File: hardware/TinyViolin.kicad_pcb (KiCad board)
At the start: 2 copper layers, 100 x 80 mm, 43 parts, among them J1 ICSP, J2 503182-1852, SW1 SW_SPDT, SW2 Tactile, SW3 SW_Push, SW4 SW_Push, SW5 SW_Push, SW6 SW_Push, U1 ATmega328-PU, U2 BOOST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

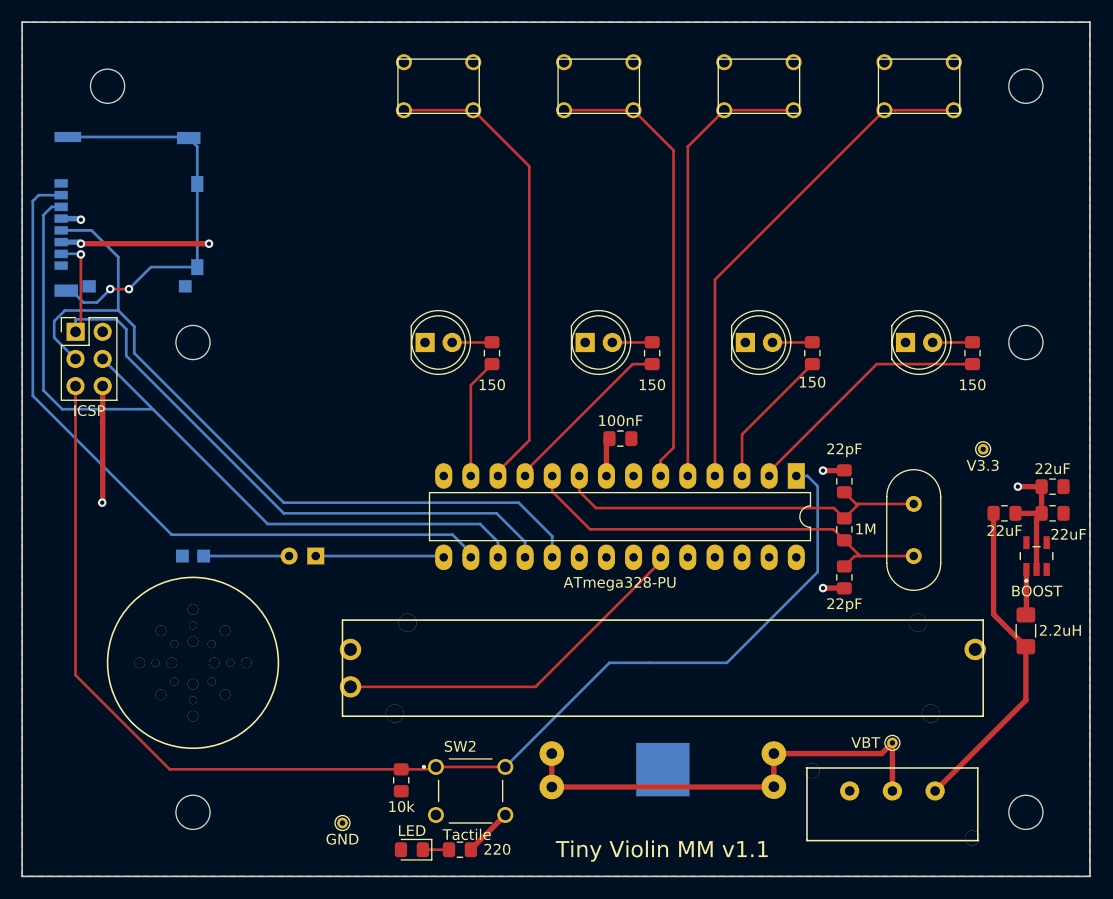
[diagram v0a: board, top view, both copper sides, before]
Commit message: Prepared pcb for re-manufacturing
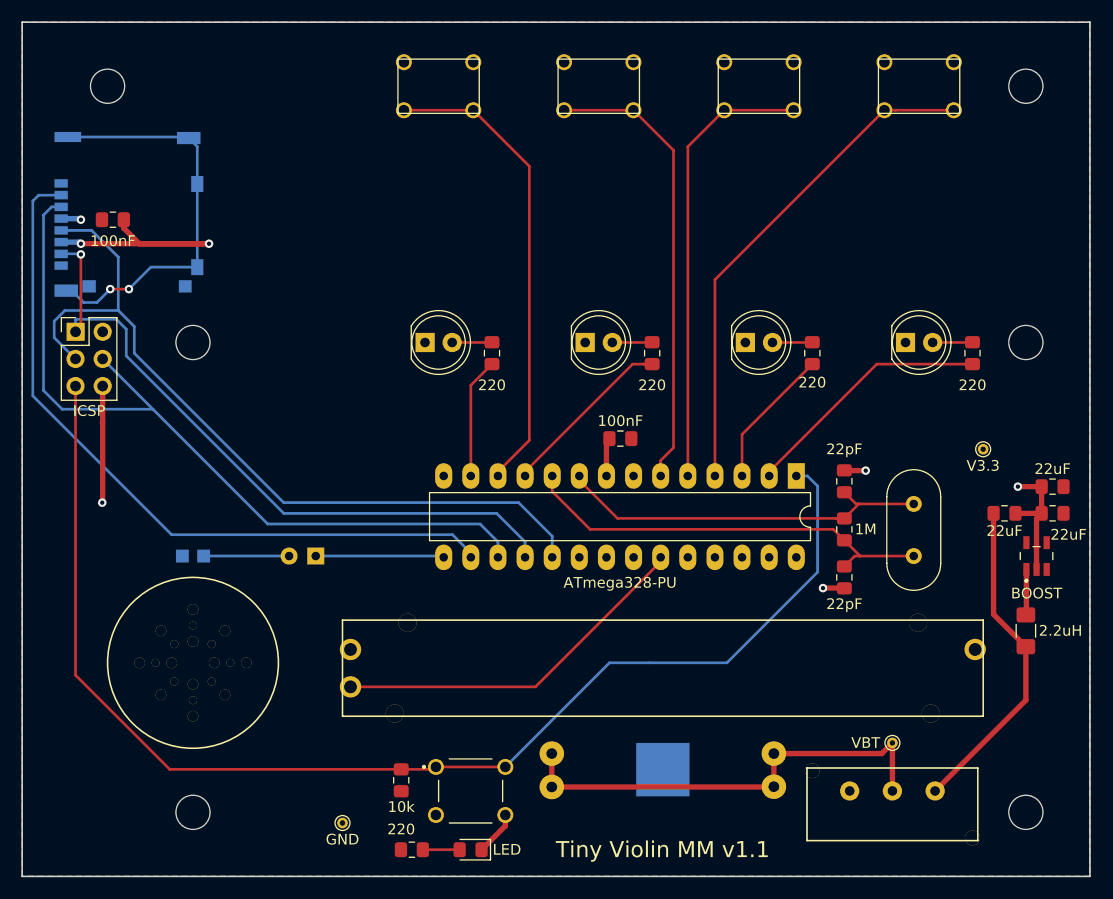
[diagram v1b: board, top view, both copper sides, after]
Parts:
- added C7: 100nF, Capacitor_SMD:C_0805_2012Metric_Pad1.15x1.40mm_HandSolder, F.Cu at (28.5, 38.5)
- BT1: footprint BAT-HLD-001-THM:LINX_BAT-HLD-001-THM -> LINX_BAT-HLD-001-THM
- J2: footprint 503182-1852:MOLEX_503182-1852 -> MOLEX_503182-1852
- R4, R5, R6, R7: value 150 -> 220
- SW2: footprint 1825910-7:SW_1825910-7 -> SW_1825910-7
- U2: footprint TPS613222ADBVT:SOT95P280X145-5N -> SOT95P280X145-5N
- moved D2 5.50 mm to (62.0, 97.5)
- moved R3 4.50 mm to (56.5, 97.5)
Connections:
- D2 pad 1: Net-(D2-Pad1) -> GND
- D2 pad 2: +3V3 -> Net-(D2-Pad2)
- H1 pad 1: (no net) -> Net-(H1-Pad1)
- H2 pad 1: (no net) -> Net-(H2-Pad1)
- H3 pad 1: (no net) -> Net-(H3-Pad1)
- H4 pad 1: (no net) -> Net-(H4-Pad1)
- H5 pad 1: (no net) -> Net-(H5-Pad1)
- H6 pad 1: (no net) -> Net-(H6-Pad1)
- J1 pad 2: (no net) -> Net-(J1-Pad2)
- J2 pad 1: (no net) -> Net-(J2-Pad1)
- J2 pad 8: (no net) -> Net-(J2-Pad8)
- J2 pad DT: (no net) -> Net-(J2-PadDT)
- J2 pad SW: (no net) -> Net-(J2-PadSW)
- R3 pad 1: Net-(D2-Pad1) -> +3V3
- R3 pad 2: GND -> Net-(D2-Pad2)
- SW1 pad 1: (no net) -> Net-(SW1-Pad1)
- U1 pad 14: (no net) -> Net-(U1-Pad14)
- U1 pad 21: (no net) -> Net-(U1-Pad21)
- U1 pad 24: (no net) -> Net-(U1-Pad24)
- U1 pad 25: (no net) -> Net-(U1-Pad25)
- U1 pad 26: (no net) -> Net-(U1-Pad26)
- U1 pad 27: (no net) -> Net-(U1-Pad27)
- U1 pad 28: (no net) -> Net-(U1-Pad28)
- U2 pad 3: (no net) -> Net-(U2-Pad3)
- U2 pad 5: (no net) -> Net-(U2-Pad5)
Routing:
- net GND: track 50.5 -> 58.9 mm
- net Net-(D2-Pad2): track 0.00 -> 3.45 mm
- net Net-(D2-Pad1): track 2.45 -> 0.00 mm
- net Net-(C2-Pad1): track 36.6 -> 35.6 mm

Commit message: Got main thing working
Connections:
- J1 pad 2: Net-(J1-Pad2) -> +3V3
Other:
- board text added: "Tiny Violin MM v1.2"
- board text removed: "Tiny Violin MM v1.1"
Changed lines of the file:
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@@
     (zones 0)
     (modules 44)
-    (nets 51)
+    (nets 50)
   )
   (page A4)
@@
   (net 41 "Net-(H1-Pad1)")
   (net 42 "Net-(SW1-Pad1)")
-  (net 43 "Net-(J1-Pad2)")
-  (net 44 "Net-(U2-Pad3)")
-  (net 45 "Net-(U2-Pad5)")
-  (net 46 "Net-(J2-Pad1)")
-  (net 47 "Net-(J2-Pad8)")
-  (net 48 "Net-(J2-PadSW)")
-  (net 49 "Net-(J2-PadDT)")
-  (net 50 "Net-(D2-Pad2)")
+  (net 43 "Net-(U2-Pad3)")
+  (net 44 "Net-(U2-Pad5)")
+  (net 45 "Net-(J2-Pad1)")
+  (net 46 "Net-(J2-Pad8)")
+  (net 47 "Net-(J2-PadSW)")
+  (net 48 "Net-(J2-PadDT)")
+  (net 49 "Net-(D2-Pad2)")
   (net_class Default "This is the default net class."
     (clearance 0.2)
@@
     (add_net "Net-(H5-Pad1)")
     (add_net "Net-(H6-Pad1)")
-    (add_net "Net-(J1-Pad2)")
     (add_net "Net-(J2-Pad1)")
     (add_net "Net-(J2-Pad8)")
@@
     (fp_circle (center -3.81 8.89) (end -3.71 8.89) (layer B.SilkS) (width 0.2))
     (pad 1 smd rect (at -2.9 6.355 270) (size 0.8 1.24) (layers B.Cu B.Paste B.Mask)
-      (net 46 "Net-(J2-Pad1)"))
+      (net 45 "Net-(J2-Pad1)"))
     (pad 2 smd rect (at -1.8 6.355 270) (size 0.8 1.24) (layers B.Cu B.Paste B.Mask)
       (net 3 /SS))
@@
       (net 4 /MISO))
     (pad 8 smd rect (at 4.8 6.355 270) (size 0.8 1.24) (layers B.Cu B.Paste B.Mask)
-      (net 47 "Net-(J2-Pad8)"))
+      (net 46 "Net-(J2-Pad8)"))
     (pad P1 smd rect (at -7.245 5.725 270) (size 0.95 2.5) (layers B.Cu B.Paste B.Mask)
       (net 16 "Net-(J2-PadP1)"))
@@
       (net 16 "Net-(J2-PadP1)"))
     (pad SW smd rect (at 6.74 3.725 270) (size 1.16 1.25) (layers B.Cu B.Paste B.Mask)
-      (net 48 "Net-(J2-PadSW)"))
+      (net 47 "Net-(J2-PadSW)"))
     (pad DT smd rect (at 6.74 -5.275 270) (size 1.16 1.2) (layers B.Cu B.Paste B.Mask)
-      (net 49 "Net-(J2-PadDT)"))
+      (net 48 "Net-(J2-PadDT)"))
     (pad P3 smd rect (at -7.145 -5.605 270) (size 1.15 2.2) (layers B.Cu B.Paste B.Mask)
       (net 16 "Net-(J2-PadP1)"))
@@
       (net 9 GND))
     (pad 3 smd rect (at 0.95 1.255) (size 0.59 1.21) (layers F.Cu F.Paste F.Mask)
-      (net 44 "Net-(U2-Pad3)"))
+      (net 43 "Net-(U2-Pad3)"))
     (pad 4 smd rect (at 0.95 -1.255 180) (size 0.59 1.21) (layers F.Cu F.Paste F.Mask)
       (net 2 +3V3))
     (pad 5 smd rect (at -0.95 -1.255 180) (size 0.59 1.21) (layers F.Cu F.Paste F.Mask)
-      (net 45 "Net-(U2-Pad5)"))
+      (net 44 "Net-(U2-Pad5)"))
   )
   (module SW_1825910-7 (layer F.Cu)
@@
       (net 5 /SCK))
     (pad 2 thru_hole oval (at 2.54 0) (size 1.7 1.7) (drill 1) (layers *.Cu *.Mask)
-      (net 43 "Net-(J1-Pad2)"))
+      (net 2 +3V3))
     (pad 1 thru_hole rect (at 0 0) (size 1.7 1.7) (drill 1) (layers *.Cu *.Mask)
       (net 4 /MISO))
@@
     (fp_line (start 1 -0.6) (end -0.7 -0.6) (layer F.Fab) (width 0.1))
     (pad 2 smd roundrect (at 1.025 0 180) (size 1.15 1.4) (layers F.Cu F.Paste F.Mask) (roundrect_rratio 0.217391)
-      (net 50 "Net-(D2-Pad2)"))
+      (net 49 "Net-(D2-Pad2)"))
     (pad 1 smd roundrect (at -1.025 0 180) (size 1.15 1.4) (layers F.Cu F.Paste F.Mask) (roundrect_rratio 0.217391)
       (net 9 GND))
@@
     (fp_line (start -1 0.6) (end -1 -0.6) (layer F.Fab) (width 0.1))
     (pad 2 smd roundrect (at 1.025 0) (size 1.15 1.4) (layers F.Cu F.Paste F.Mask) (roundrect_rratio 0.217391)
-      (net 50 "Net-(D2-Pad2)"))
+      (net 49 "Net-(D2-Pad2)"))
     (pad 1 smd roundrect (at -1.025 0) (size 1.15 1.4) (layers F.Cu F.Paste F.Mask) (roundrect_rratio 0.217391)
       (net 2 +3V3))
@@
   )
   (gr_line (start 20 20) (end 120 20) (layer Edge.Cuts) (width 0.15))
-  (gr_text "Tiny Violin MM v1.1" (at 80 97.5) (layer F.SilkS)
+  (gr_text "Tiny Violin MM v1.2" (at 80 97.5) (layer F.SilkS)
     (effects (font (size 1.5 1.5) (thickness 0.3)))
   )
@@
   (segment (start 114.05 75.4625) (end 114 75.5125) (width 0.5) (layer F.Cu) (net 28))
   (segment (start 114.05 71.255) (end 114.05 75.4625) (width 0.5) (layer F.Cu) (net 28))
-  (segment (start 57.525 97.5) (end 60.975 97.5) (width 0.25) (layer F.Cu) (net 50))
+  (segment (start 57.525 97.5) (end 60.975 97.5) (width 0.25) (layer F.Cu) (net 49))
   (zone (net 2) (net_name +3V3) (layer F.Cu) (hatch edge 0.508)
     (connect_pads (clearance 0.508))

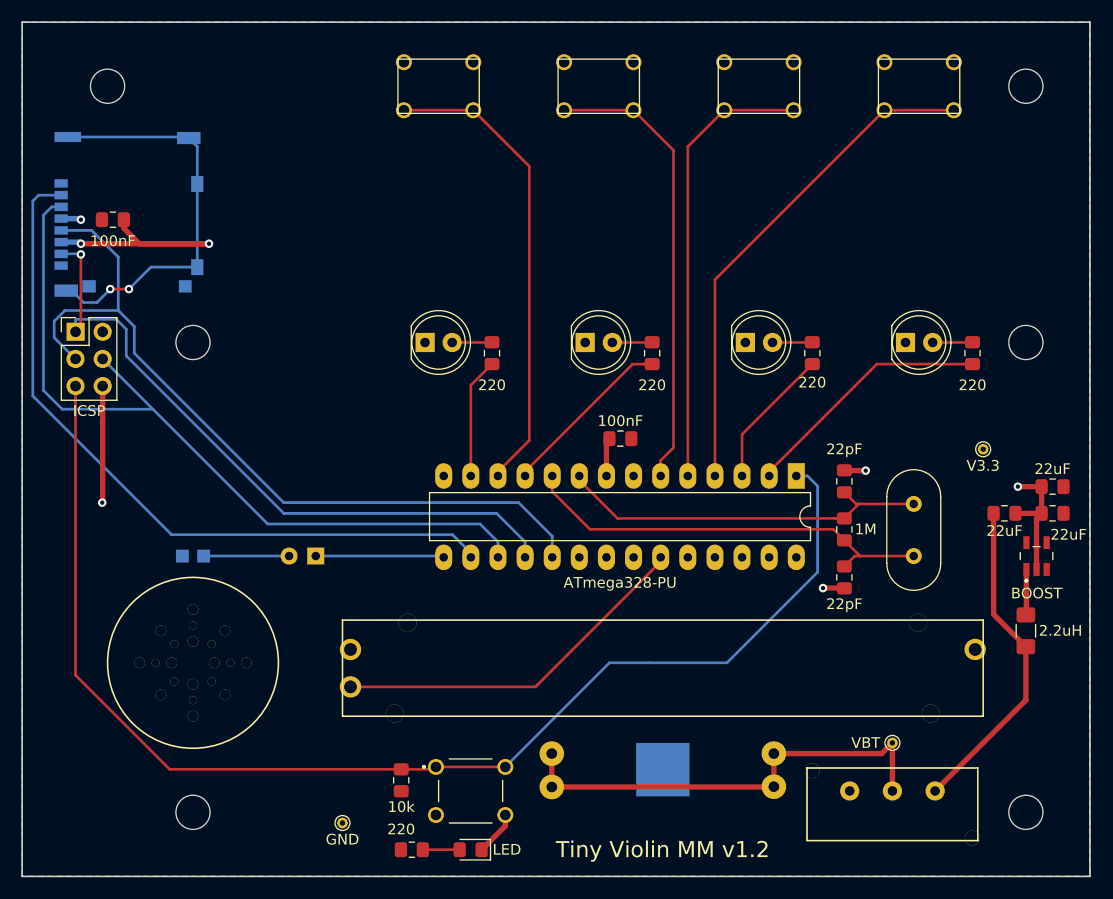
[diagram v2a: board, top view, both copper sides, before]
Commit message: Changed battery on PCB
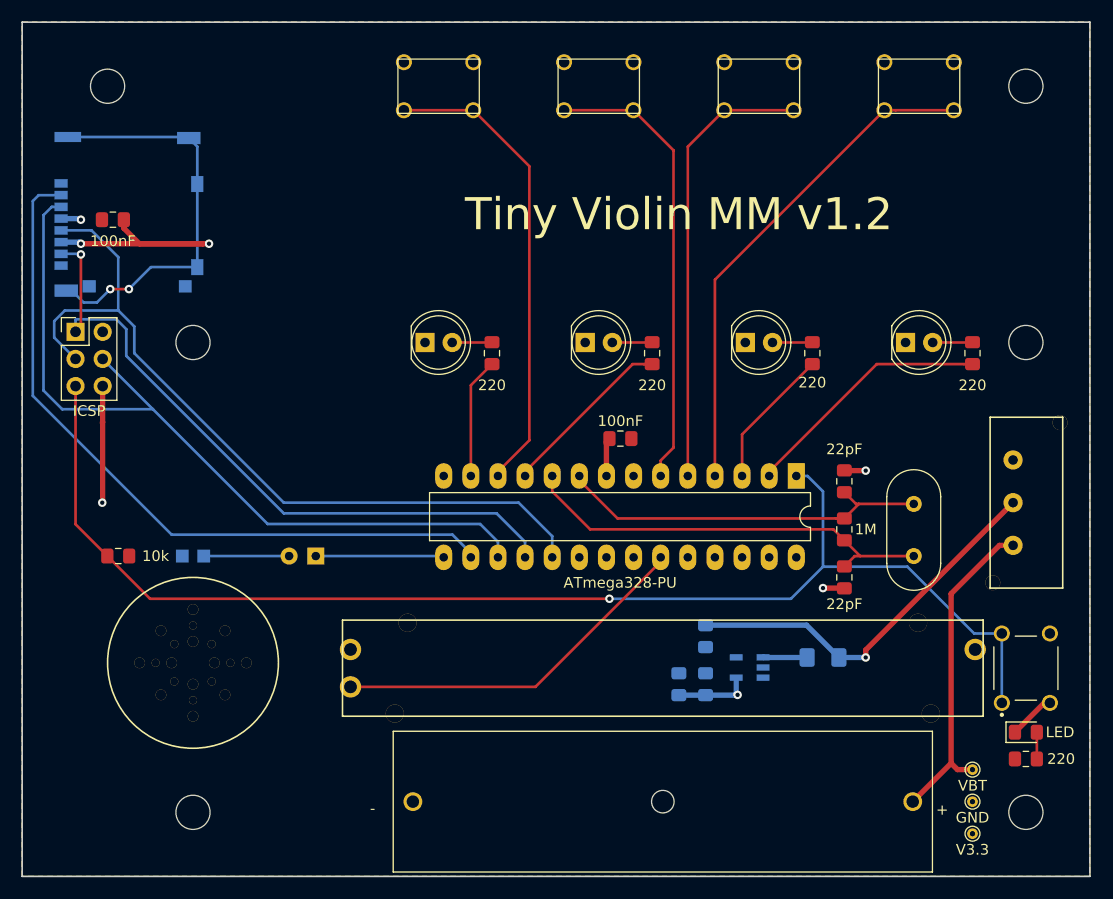
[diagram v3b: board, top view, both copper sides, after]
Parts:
- BT1: value BAT-HLD-001-THM -> BCAAAPC; footprint LINX_BAT-HLD-001-THM -> BAT_BCAAAPC; moved to F.Cu
- C4, C5, C6, L1, U2: moved to B.Cu
- Y1: value Crystal 16MHz -> Crystal 8MHz
- moved TP2 59.0 mm to (109.0, 93.0)
- moved R3 58.1 mm to (114.0, 89.0)
- moved SW2 53.3 mm to (114.0, 80.5), turned to 90 degrees
- moved D2 53.2 mm to (114.0, 86.5), turned to 0 degrees
- moved C5 39.6 mm to (81.5, 82.0), turned to 90 degrees
- moved C6 36.2 mm to (84.0, 82.0), turned to 90 degrees
- moved TP3 36.0 mm to (109.0, 96.0)
- moved R2 33.8 mm to (29.0, 70.0), turned to 180 degrees
- moved C4 30.3 mm to (84.0, 77.5), turned to 270 degrees
- moved SW1 29.3 mm to (112.8, 65.0), turned to 180 degrees
- moved U2 28.8 mm to (88.1, 80.4), turned to 270 degrees
- moved L1 19.2 mm to (95.0, 79.5), turned to 180 degrees
- moved TP1 7.91 mm to (109.0, 90.0)
- moved BT1 3.00 mm to (80.0, 93.0), turned to 0 degrees
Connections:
- SW1 pad 1: Net-(SW1-Pad1) -> /BAT
- SW1 pad 2: /BAT -> /BAT1
- SW1 pad 3: /BAT1 -> Net-(SW1-Pad3)
- U1 pad 20: +3V3 -> Net-(U1-Pad20)
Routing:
- net GND: track 58.9 -> 46.5 mm, vias 6 -> 5
- net /BAT: track 43.1 -> 30.9 mm
- net +3V3: track 1.90 -> 9.13 mm, vias 1 -> 2
- net /BAT1: track 30.8 -> 36.5 mm, vias 0 -> 1
- net /~RST: track 118.3 -> 123.1 mm, vias 0 -> 1
- net /PB2: track 44.3 -> 42.8 mm
- net Net-(D2-Pad2): track 3.45 -> 2.50 mm
